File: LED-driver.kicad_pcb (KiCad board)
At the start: 2 copper layers, 60.1 x 81.9 mm, 38 parts, among them J1 Screw_Terminal_1x02, J2 PIC Kit3 header, J3 Screw_Terminal_1x02, J4 Screw_Terminal_1x02, J5 Screw_Terminal_1x02, J6 Screw_Terminal_1x03, Q1 2N7002, Q2 2N7002, Q3 BSS123, U1 PIC12F1572, U2 CAT4101, U3 MAX485, U4 CAT4101, U5 CAT4101

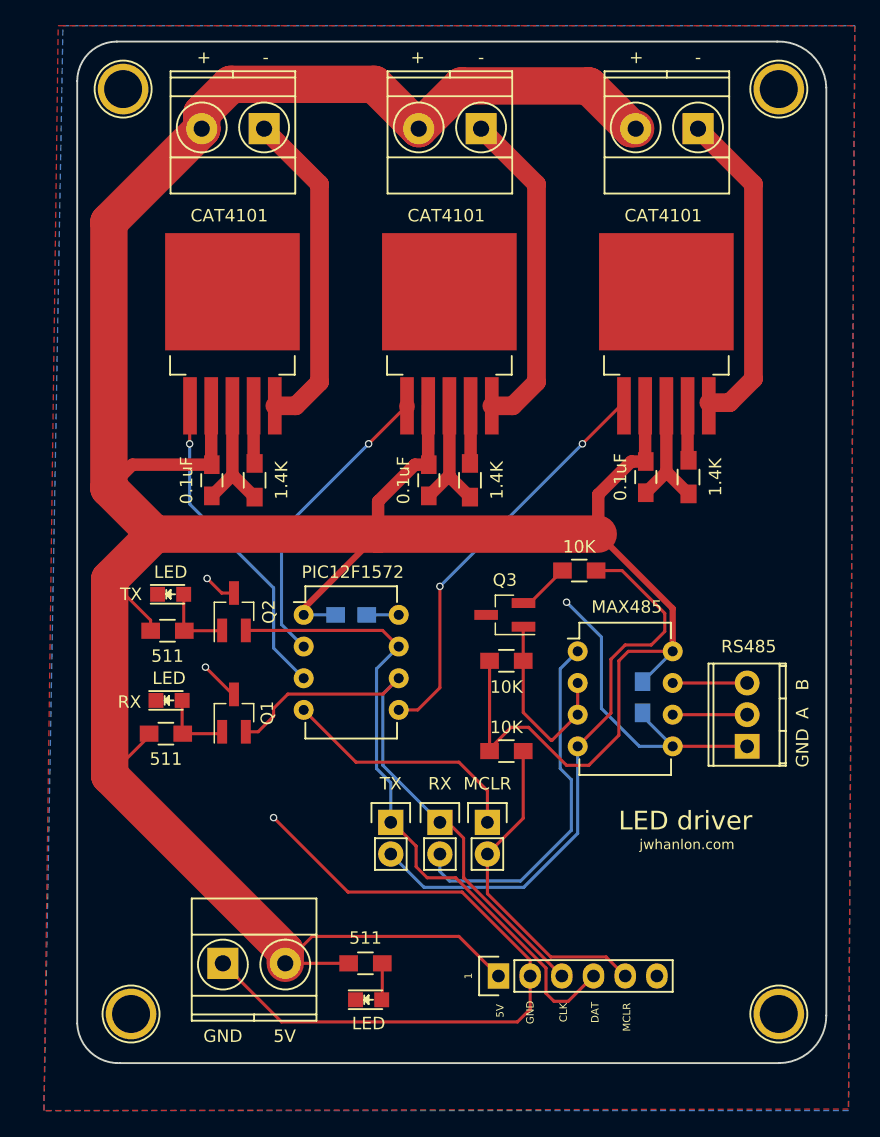
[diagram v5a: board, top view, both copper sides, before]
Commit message: Fix pins of FETs and other board tweaks.
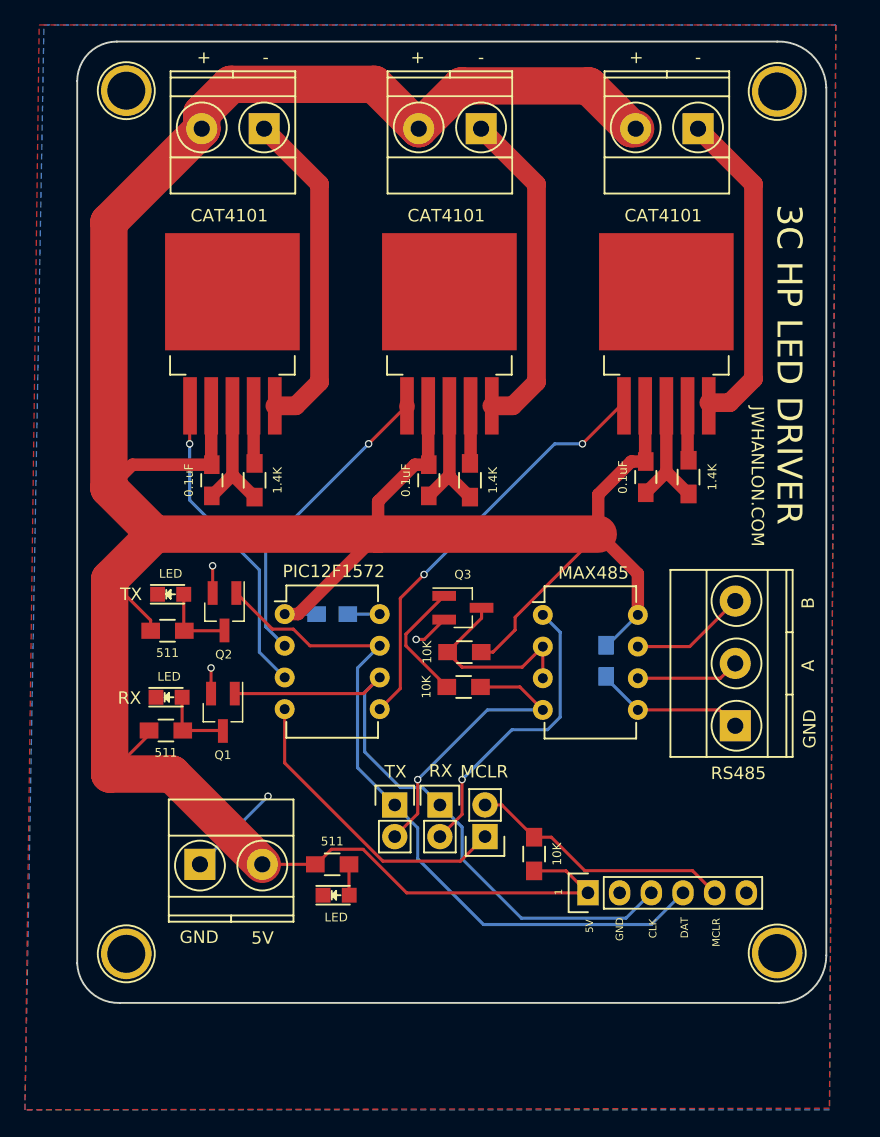
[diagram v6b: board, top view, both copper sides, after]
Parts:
- J6: footprint Connectors_Terminal_Blocks:TerminalBlock_Pheonix_MPT-2.54mm_3pol -> Connectors_Terminal_Blocks:TerminalBlock_Pheonix_MKDS1.5-3pol
- Q3: value BSS123 -> 2N7002
- moved R8 13.2 mm to (158.2, 79.1)
- moved J2 9.80 mm to (168.2, 95.6)
- moved D2 8.78 mm to (148.0, 95.8)
- moved R7 8.55 mm to (163.9, 92.5), turned to 90 degrees
- moved R6 8.37 mm to (147.7, 93.3)
- moved J5 8.15 mm to (137.1, 93.3)
- moved REF** 4.89 mm to (183.4, 100.4)
- moved REF** 4.84 mm to (131.2, 100.5)
- moved 0.1uF4 4.13 mm to (169.7, 77.0)
- moved U3 4.04 mm to (164.6, 73.3)
- moved R9 3.44 mm to (158.3, 76.3), turned to 180 degrees
- moved Q3 3.41 mm to (158.2, 72.7), turned to 0 degrees
- moved J6 1.91 mm to (180.0, 82.2)
- moved 0.1uF3 1.53 mm to (147.7, 73.2)
- moved U1 1.53 mm to (143.9, 73.2)
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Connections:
- Q1 pad 1: Net-(D1-Pad2) -> UART_RX/CLK
- Q1 pad 2: UART_RX/CLK -> GND
- Q1 pad 3: GND -> Net-(D1-Pad2)
- Q2 pad 1: Net-(D3-Pad2) -> UART_TX/DAT
- Q2 pad 2: UART_TX/DAT -> GND
- Q2 pad 3: GND -> Net-(D3-Pad2)
- Q3 pad 2: Net-(Q3-Pad2) -> GND
- Q3 pad 3: GND -> Net-(Q3-Pad3)
- R8 pad 1: Net-(Q3-Pad2) -> Net-(Q3-Pad1)
- R9 pad 2: Net-(Q3-Pad1) -> Net-(Q3-Pad3)
- U3 pad 2: Net-(Q3-Pad1) -> Net-(Q3-Pad3)
- U3 pad 3: Net-(Q3-Pad1) -> Net-(Q3-Pad3)
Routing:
- net GND: track 122.7 -> 60.6 mm
- net Net-(JP3-Pad2): track 46.6 -> 23.4 mm, vias 0 -> 1
- net Net-(Q3-Pad3): track 0.00 -> 16.1 mm
- net +5V: track 287.8 -> 271.8 mm
- net Net-(Q3-Pad1): track 15.5 -> 9.96 mm
- net Net-(JP2-Pad2): track 29.2 -> 24.0 mm, vias 0 -> 1
- net UART_RX/CLK: track 45.1 -> 50.1 mm
- net Net-(J2-Pad5): track 26.5 -> 21.8 mm
- net UART_TX/DAT: track 53.2 -> 57.9 mm
- net MCLR: track 20.0 -> 24.5 mm
- net Net-(Q3-Pad2): track 4.20 -> 0.00 mm
- net Net-(J6-Pad3): track 5.97 -> 9.32 mm
- net Net-(J6-Pad2): track 5.97 -> 8.30 mm
- net Net-(U1-Pad5): track 33.0 -> 34.0 mm
- net Net-(U1-Pad3): track 25.7 -> 25.0 mm
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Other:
- board size 60.1 x 81.9 mm -> 60.1 x 77.1 mm
- board text added: "3C HP LED DRIVER"
- board text added: "JWHANLON.COM"
- board text removed: "LED driver"
- board text removed: "jwhanlon.com"

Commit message: Final tweaks for version 2.
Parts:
- moved D2 14.9 mm to (133.2, 94.7), turned to 180 degrees
- moved R6 14.3 mm to (133.5, 91.8), turned to 180 degrees
- moved J2 4.79 mm to (163.7, 97.3)
- moved R9 3.94 mm to (159.0, 72.4), turned to 0 degrees
- moved J5 3.70 mm to (140.1, 95.4)
- moved Q3 3.15 mm to (159.0, 75.7)
- moved R7 2.54 mm to (163.8, 89.9)
- moved R8 0.77 mm to (159.0, 79.2)
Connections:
- J2 pad 1: +5V -> MCLR
- J2 pad 2: GND -> +5V
- J2 pad 3: UART_RX/CLK -> GND
- J2 pad 5: Net-(J2-Pad5) -> UART_RX/CLK
- JP1 pad 2: Net-(J2-Pad5) -> Net-(JP1-Pad2)
- R7 pad 2: Net-(J2-Pad5) -> Net-(JP1-Pad2)
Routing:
- net Net-(J2-Pad5): track 21.8 -> 0.00 mm
- net MCLR: track 24.5 -> 32.3 mm
- net GND: track 60.6 -> 53.5 mm, vias 4 -> 3
- net +5V: track 271.8 -> 278.0 mm
- net Net-(Q3-Pad3): track 16.1 -> 10.1 mm
- net UART_TX/DAT: track 57.9 -> 52.0 mm
- net Net-(U1-Pad3): track 25.0 -> 29.3 mm
- net Net-(JP1-Pad2): track 0.00 -> 3.83 mm
- net Net-(Q3-Pad1): track 9.96 -> 11.5 mm
- net Net-(JP2-Pad2): track 24.0 -> 25.4 mm
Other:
- board text added: "POWER"
- board text added: "Pin 1"
- board text removed: "1"
